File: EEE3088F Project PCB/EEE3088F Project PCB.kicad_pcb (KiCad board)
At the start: 2 copper layers, 80 x 54.9 mm, 80 parts, among them J1 JST PH 2.00mm connector, Q1 NPN, SW1 SS-12D10L3, U1 DRV8833PWR, U10 LM7805L-TF3-T, U11 TC4056A., U2 DRV8833PWPR, U3 INA219AxD, U4 CH224K, U6 MIC5504-1.2YM5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

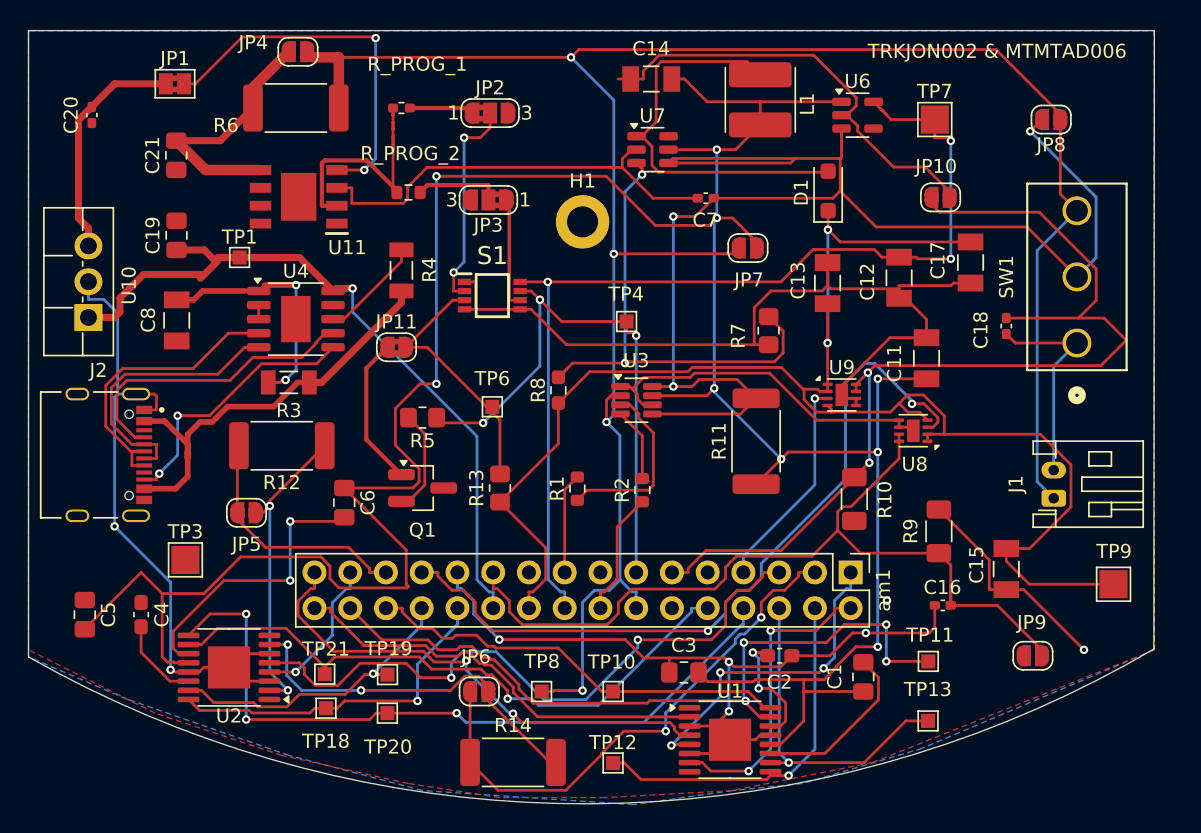
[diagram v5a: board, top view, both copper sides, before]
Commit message: finshed routing for Jonathan and half of Tadalas routing
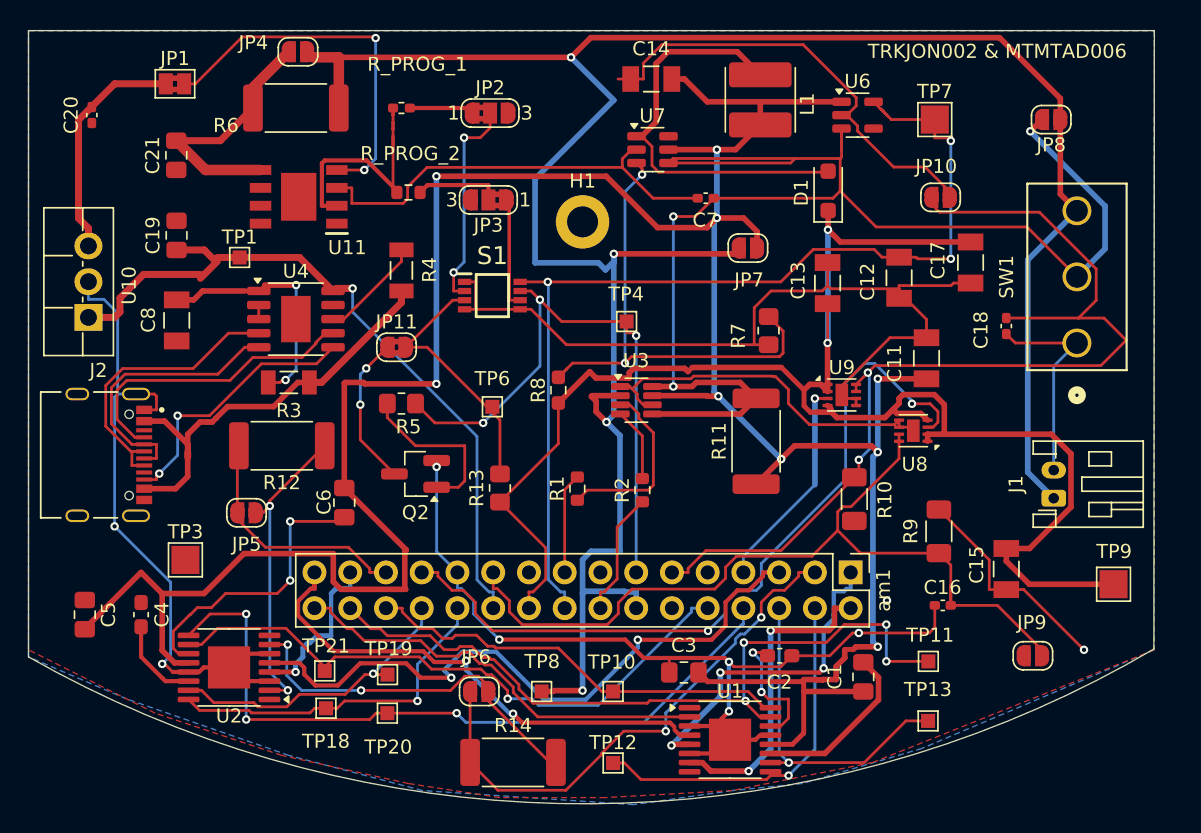
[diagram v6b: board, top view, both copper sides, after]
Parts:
- removed Q1: NPN, Package_TO_SOT_SMD:SOT-23_Handsoldering
- added Q2: NPN, Package_TO_SOT_SMD:SOT-23_Handsoldering, F.Cu at (179.0, 109.0)
- moved R5 1.80 mm to (178.0, 104.0)
- moved TP21 0.23 mm to (172.6, 123.0)
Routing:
- net /Battery: track 154.8 -> 170.9 mm
- net GND: track 286.4 -> 297.2 mm, vias 8 -> 9
- net Net-(Q2-B): track 7.41 -> 12.0 mm
- net /5V Out: track 111.5 -> 114.6 mm
- net /V_sensing: track 208.6 -> 211.2 mm
- net /FAST_CHARGE_CTRL: track 40.7 -> 42.7 mm
- net /MOTOR3_B_OUT: track 10.7 -> 11.8 mm
- net Net-(U1-VINT): track 8.71 -> 9.43 mm
- net Net-(D1-A): track 28.8 -> 29.5 mm
- net /CTRL_EXT_LOAD1: track 54.9 -> 55.5 mm
- net /Motor2_A_OUT: track 21.6 -> 22.1 mm
- net Net-(JP11-A): track 10.7 -> 10.8 mm, vias 0 -> 2

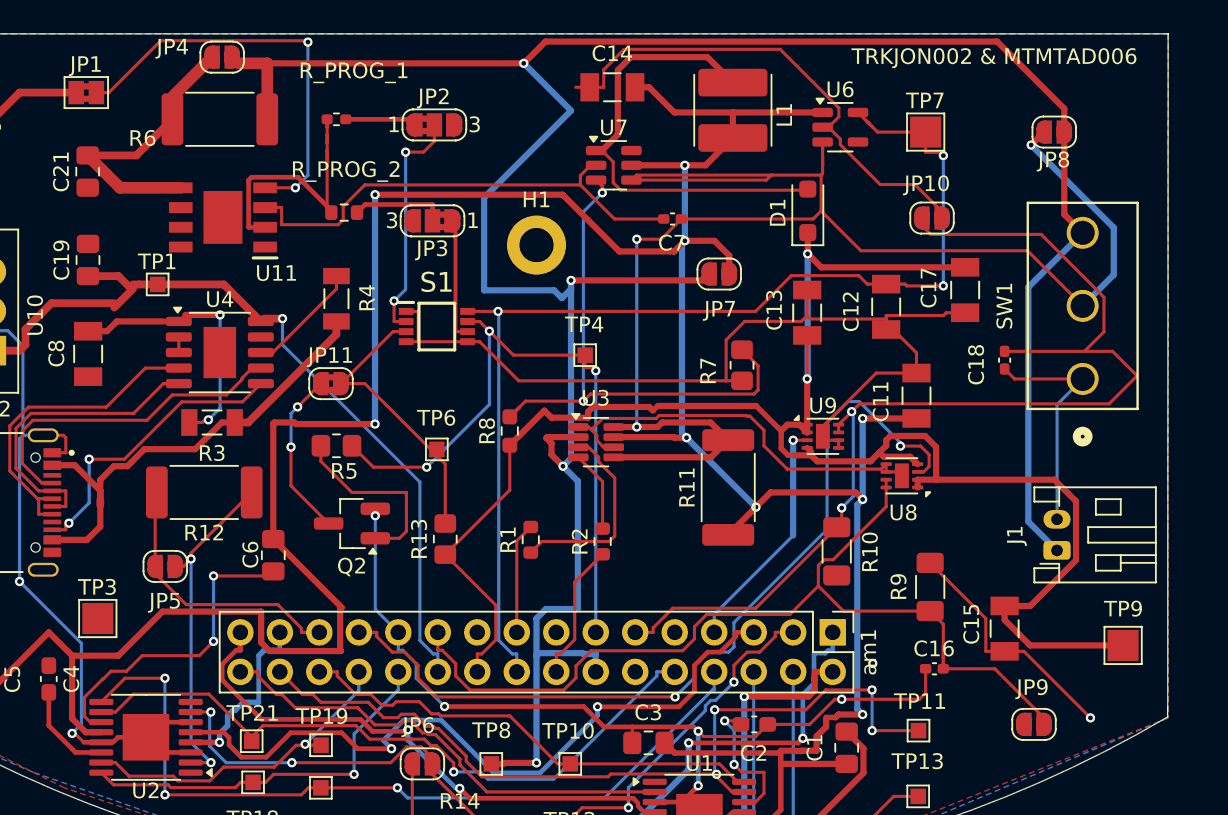
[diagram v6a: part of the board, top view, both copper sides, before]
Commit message: adjusted wiring width
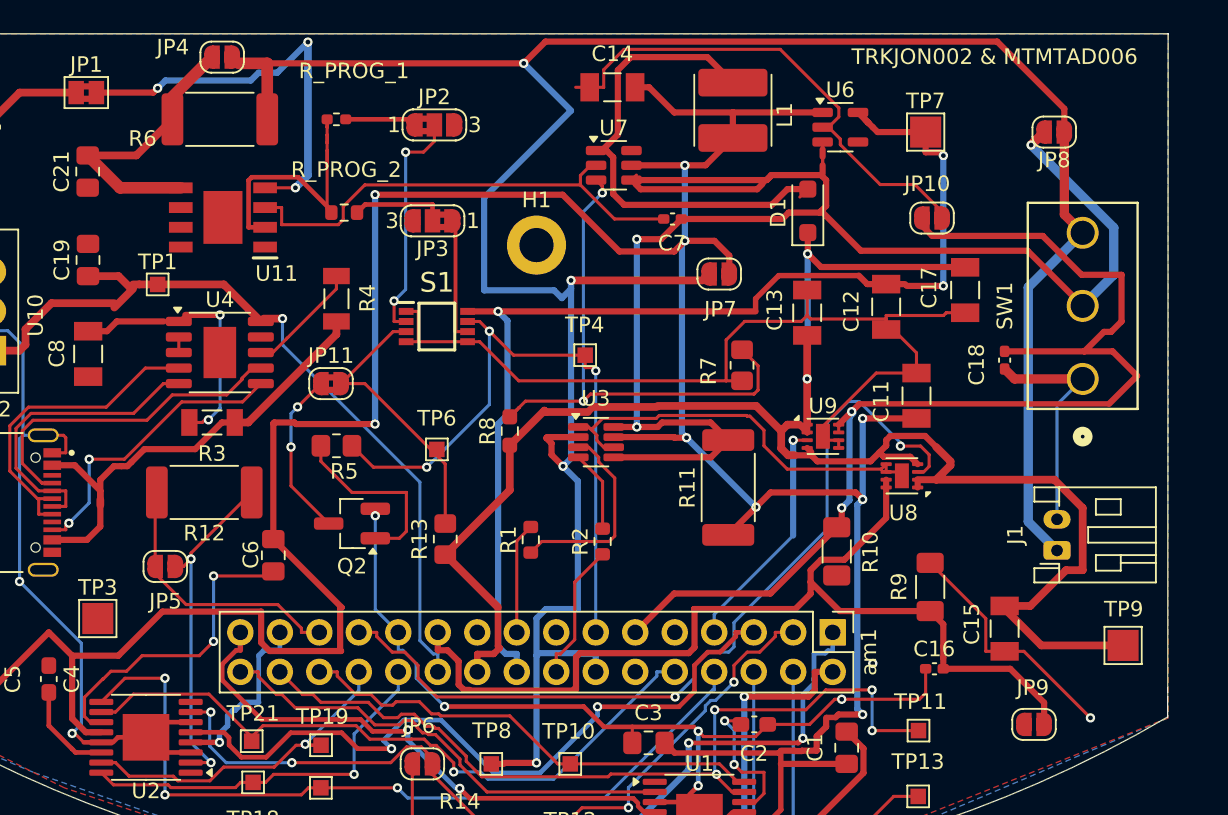
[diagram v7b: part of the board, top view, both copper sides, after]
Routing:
- net /EXT_LOAD1_OUT: track 61.4 -> 65.4 mm
- net /EXT_LOAD2_OUT: track 72.1 -> 74.7 mm
- net Net-(D1-A): track 29.5 -> 32.0 mm
- net /3V3 Out: track 72.3 -> 73.5 mm
- net /5V Out: track 114.6 -> 115.9 mm
- net /V_switch: track 101.1 -> 102.3 mm
- net Net-(JP1-B): vias 2 -> 3

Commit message: passed all DRC's
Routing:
- net GND: track 297.2 -> 318.9 mm, vias 9 -> 13
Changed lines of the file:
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@@
 		(tags "test point SMD pad rectangle square")
 		(property "Reference" "TP1"
-			(at 0 -1.448 0)
+			(at -1 -1.448 0)
 			(layer "F.SilkS")
 			(effects
@@
 		(layer "Margin")
 		(pts
+			(xy 190.87 117.275) (xy 190.87 91.09)
+		)
+		(height -80.87)
+		(orientation 1)
+		(format
+			(prefix "")
+			(suffix "")
+			(units 3)
+			(units_format 0)
+			(precision 4)
+			(suppress_zeroes yes)
+		)
+		(style
+			(thickness 0.1)
+			(arrow_length 1.27)
+			(text_position_mode 0)
+			(arrow_direction outward)
+			(extension_height 0.58642)
+			(extension_offset 0.5)
+			(keep_text_aligned yes)
+		)
+		(gr_text "26.185"
+			(at 108.85 104.1825 90)
+			(layer "Margin")
+			(effects
+				(font
+					(size 1 1)
+					(thickness 0.15)
+				)
+			)
+		)
+	)
+	(dimension
+		(type orthogonal)
+		(layer "Margin")
+		(pts
 			(xy 190.87 117.2) (xy 190.3 132.425)
 		)
@@
 	)
 	(segment
+		(start 163.713 95.105896)
+		(end 164.919 93.899896)
+		(width 0.5)
+		(layer "F.Cu")
+		(net 16)
+	)
+	(segment
 		(start 165.32 93.62)
 		(end 164.919 93.62)
@@
 	)
 	(segment
+		(start 163.713 95.105975)
+		(end 163.713 95.105896)
+		(width 0.5)
+		(layer "F.Cu")
+		(net 16)
+	)
+	(segment
 		(start 173.149 95.9886)
 		(end 173.1435 95.9943)
@@
 	)
 	(segment
-		(start 163.713 95.105975)
-		(end 164.919 93.899875)
+		(start 157.62 97.88)
+		(end 158 97.5)
 		(width 0.5)
 		(layer "F.Cu")
@@
 	)
 	(segment
-		(start 157.62 97.88)
-		(end 158 97.5)
+		(start 164.919 93.899896)
+		(end 164.919 93.899875)
 		(width 0.5)
 		(layer "F.Cu")
@@
 	)
 	(segment
+		(start 157.66 95.34)
+		(end 155.76 95.34)
+		(width 0.2)
+		(layer "F.Cu")
+		(net 17)
+	)
+	(segment
 		(start 182.485 95.355)
 		(end 182.873 95.355)
@@
 	)
 	(segment
+		(start 159.5 117)
+		(end 159.5 118.1375)
+		(width 0.2)
+		(layer "F.Cu")
+		(net 17)
+	)
+	(segment
 		(start 163.623 123.075)
 		(end 162.875 123.075)
@@
 	)
 	(segment
+		(start 175 92.5)
+		(end 175 90.5)
+		(width 0.2)
+		(layer "F.Cu")
+		(net 17)
+	)
+	(segment
 		(start 183.262 97.305)
 		(end 182.485 97.305)
@@
 	)
 	(segment
+		(start 175 90.5)
+		(end 175.5 90)
+		(width 0.2)
+		(layer "F.Cu")
+		(net 17)
+	)
+	(segment
 		(start 204.261 95.9983)
 		(end 203.067 97.1925)
@@
 	)
 	(segment
+		(start 161.9875 91.0125)
+		(end 157.66 95.34)
+		(width 0.2)
+		(layer "F.Cu")
+		(net 17)
+	)
+	(segment
 		(start 214.122 105.68)
 		(end 214.372 105.93)
@@
 	)
 	(segment
+		(start 162.02 91.0125)
+		(end 161.9875 91.0125)
+		(width 0.2)
+		(layer "F.Cu")
+		(net 17)
+	)
+	(segment
 		(start 215.31 99.06)
 		(end 215.31 99.32)
@@
 	)
 	(via
+		(at 159.5 117)
+		(size 0.6)
+		(drill 0.3)
+		(layers "F.Cu" "B.Cu")
+		(net 17)
+	)
+	(via
 		(at 212.5 118)
 		(size 0.6)
@@
 	)
 	(via
+		(at 171.5 96)
+		(size 0.6)
+		(drill 0.3)
+		(layers "F.Cu" "B.Cu")
+		(free yes)
+		(net 17)
+	)
+	(via
 		(at 210.5 120.303)
 		(size 0.6)
@@
 	)
 	(via
+		(at 175 92.5)
+		(size 0.6)
+		(drill 0.3)
+		(layers "F.Cu" "B.Cu")
+		(free yes)
+		(net 17)
+	)
+	(via
+		(at 175.5 90)
+		(size 0.6)
+		(drill 0.3)
+		(layers "F.Cu" "B.Cu")
+		(net 17)
+	)
+	(via
 		(at 201.271 125.87)
 		(size 0.6)
@@
 	)
 	(segment
+		(start 160.5 117)
+		(end 159.5 117)
+		(width 0.2)
+		(layer "B.Cu")
+		(net 17)
+	)
+	(segment
 		(start 159.14 103.325)
 		(end 157.838 103.325)
@@
 	)
 	(segment
+		(start 171.5 96)
+		(end 175.5 92)
+		(width 0.4)
+		(layer "B.Cu")
+		(net 17)
+	)
+	(segment
 		(start 161.595 121.905)
 		(end 161.595 116.704)
@@
 	)
 	(segment
+		(start 160.796 116.704)
+		(end 160.5 117)
+		(width 0.2)
+		(layer "B.Cu")
+		(net 17)
+	)
+	(segment
 		(start 161 122.5)
 		(end 161.595 121.905)
@@
 	)
 	(segment
+		(start 161.595 116.704)
+		(end 160.796 116.704)
+		(width 0.2)
+		(layer "B.Cu")
+		(net 17)
+	)
+	(segment
 		(start 155.76 96.5942)
 		(end 156.855 96.5942)
@@
 		(layer "B.Cu")
 		(net 17)
+	)
+	(segment
+		(start 175.5 92)
+		(end 175.5 90)
+		(width 0.4)
+		(layer "B.Cu")
+		(net 17)
